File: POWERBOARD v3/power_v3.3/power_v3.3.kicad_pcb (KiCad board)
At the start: 2 copper layers, 46 parts, among them IC1 MAX25301AATB_V+T, J1 2053380003, J2 UJ20-C-H-G-SMT-1-P16-TR, J3 2053380002, U1 USBLC6-2, U2 BQ25886RGE, U3 TPS62160DSG

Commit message: (nearly) finished schematic and layout, beginning routing (hooooooly)
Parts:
- removed C9: 22u, Capacitor_SMD:C_1206_3216Metric
- added C14: 100n, Capacitor_SMD:C_0402_1005Metric, F.Cu at (151.0, 88.2)
- added C15: 100n, Capacitor_SMD:C_0402_1005Metric, F.Cu at (153.5, 88.2)
- added C16: 100n, Capacitor_SMD:C_0402_1005Metric, F.Cu at (151.0, 80.8)
- added C17: 100n, Capacitor_SMD:C_0402_1005Metric, F.Cu at (142.0, 73.0)
- added D5: LED, LED_THT:LED_D5.0mm, F.Cu at (155.5, 72.5)
- added IC2: MCP6541T-I_OT, MCP6541T-I_OT:SOT95P270X145-5N, F.Cu at (152.0, 84.5)
- added IC3: AP2281-1FMG-7, APP2281-1FMG-7:SON50P201X181X60-7N, F.Cu at (142.0, 76.0)
- added R13: 10k, Resistor_SMD:R_0603_1608Metric, B.Cu at (148.5, 94.0)
- added R14: 51.1k, Resistor_SMD:R_0603_1608Metric, B.Cu at (152.2, 79.8)
- added R15: 10k, Resistor_SMD:R_0603_1608Metric, B.Cu at (149.0, 84.2)
- added R16: 26.7k, Resistor_SMD:R_0603_1608Metric, B.Cu at (149.0, 88.1)
- added R17: 10k, Resistor_SMD:R_0603_1608Metric, B.Cu at (147.0, 85.9)
- added R18: 330, Resistor_SMD:R_0603_1608Metric, B.Cu at (156.2, 77.8)
- added S2: MFS201N-9-Z, MFS201N-9-Z:MFS201N9Z, F.Cu at (156.0, 101.0)
- D3, D4, R1, R10, R11, R12, R2, R3, R4, R5, R6, R7: moved to B.Cu
- moved BAT1 48.5 mm to (136.5, 98.0), turned to 180 degrees
- moved J1 39.3 mm to (135.3, 89.7), turned to 90 degrees
- moved GND1 37.9 mm to (186.5, 99.5), turned to 180 degrees
- moved LDO5V1 35.9 mm to (147.0, 72.0), turned to 180 degrees
- moved R12 35.3 mm to (169.8, 92.0)
- moved R11 32.9 mm to (166.9, 87.5), turned to 90 degrees
- moved R10 32.0 mm to (166.9, 91.3), turned to 90 degrees
- moved R1 31.2 mm to (182.5, 96.3), turned to -90 degrees
- moved J3 31.2 mm to (135.2, 76.3), turned to 90 degrees
- moved L2 29.7 mm to (169.9, 93.0), turned to 180 degrees
- moved C12 29.3 mm to (158.5, 85.0), turned to 90 degrees
- moved C11 27.6 mm to (159.5, 90.5), turned to -90 degrees
- moved Cout1 27.2 mm to (172.9, 87.5), turned to 90 degrees
- moved C10 27.0 mm to (163.1, 85.5), turned to 180 degrees
- moved U1 26.9 mm to (187.0, 80.0), turned to 90 degrees
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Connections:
- net /Charging circuit/NTC renamed NTC
- J3 pad 1: /5.3 to 5V/output_at_5 -> Net-(IC3-OUT_1)
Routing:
- net /5.3 to 5V/INCOMP: track 0.00 -> 28.0 mm
- net /5.3 to 5V/output_at_5: track 0.00 -> 25.1 mm, vias 0 -> 2
- net VBUS: track 0.00 -> 17.5 mm
- net /Charging circuit/BATTERY VOLTAGE: track 0.00 -> 11.0 mm
- net /5.3 to 5V/IN: track 0.00 -> 10.5 mm, vias 0 -> 1
- net /Charging circuit/REGN: track 0.00 -> 7.54 mm, vias 0 -> 1
- net NTC: track 0.00 -> 7.02 mm, vias 0 -> 1
- net /Charging circuit/PMID: track 0.00 -> 6.86 mm
- net /Charging circuit/SYS: track 0.00 -> 5.17 mm
- net Net-(D5-K): track 0.00 -> 4.80 mm
- net Net-(U3-FB): track 0.00 -> 4.73 mm, vias 0 -> 1
- net /Charging circuit/ICHGSET: track 0.00 -> 4.67 mm, vias 0 -> 1
- net Net-(IC3-OUT_1): track 0.00 -> 4.60 mm
- net Net-(U3-SW): track 0.00 -> 4.26 mm
- net Net-(U3-PG): track 0.00 -> 4.22 mm, vias 0 -> 1
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- added copper zone on In1.Cu, net GND
- added copper zone on In2.Cu, net GND
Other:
- copper layers 2 -> 4

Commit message: updated routing
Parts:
- moved BAT1 12.8 mm to (126.8, 106.4)
- moved LDO5V1 11.1 mm to (143.2, 82.4), turned to 0 degrees
- moved BUCK5V3 10.3 mm to (169.4, 107.0)
- moved R9 9.17 mm to (188.0, 79.0), turned to 90 degrees
- moved SYS1 8.73 mm to (176.8, 106.6)
- moved R8 7.59 mm to (186.2, 79.0), turned to 90 degrees
- moved D2 6.52 mm to (188.0, 82.2), turned to 90 degrees
- moved GND1 6.20 mm to (188.4, 105.4)
- moved U1 4.97 mm to (182.1, 79.5), turned to -90 degrees
- moved R13 4.09 mm to (147.0, 90.2)
- moved D1 3.42 mm to (186.2, 82.2), turned to -90 degrees
- moved S2 3.17 mm to (155.7, 97.8)
- moved R3 1.62 mm to (184.8, 78.8)
- moved R4 1.17 mm to (178.6, 97.8)
- moved R1 1.05 mm to (182.5, 97.4)
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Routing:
- net /5.3 to 5V/output_at_5: track 25.1 -> 53.1 mm, vias 2 -> 4
- net /5.3 to 5V/INCOMP: track 28.0 -> 11.4 mm
- net /Charging circuit/SW: track 1.43 -> 18.0 mm, vias 0 -> 2
- net /5.3 to 5V/switch_out: track 3.68 -> 18.8 mm, vias 0 -> 2
- net VBUS: track 17.5 -> 3.00 mm
- net GND: track 1.50 -> 10.7 mm, vias 0 -> 47
- net Net-(S1-COM): track 0.00 -> 7.92 mm
- net /Charging circuit/BATTERY VOLTAGE: track 11.0 -> 3.77 mm
- net Net-(IC2-VIN-): track 2.98 -> 7.49 mm, vias 0 -> 1
- net Net-(U3-SW): track 4.26 -> 0.00 mm
- net Net-(S2-NC_2): track 3.88 -> 0.71 mm
- net Net-(J2-DP1): track 0.00 -> 2.88 mm
- net /Charging circuit/ILIM: track 2.53 -> 5.30 mm
- net Net-(J2-DN1): track 0.00 -> 2.62 mm
- net Net-(D2-A): track 2.50 -> 0.00 mm
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- added copper zone on F.Cu, net /5.3 to 5V/IN
- added copper zone on F.Cu, net Net-(U3-SW)
- removed copper zone on In2.Cu, net GND

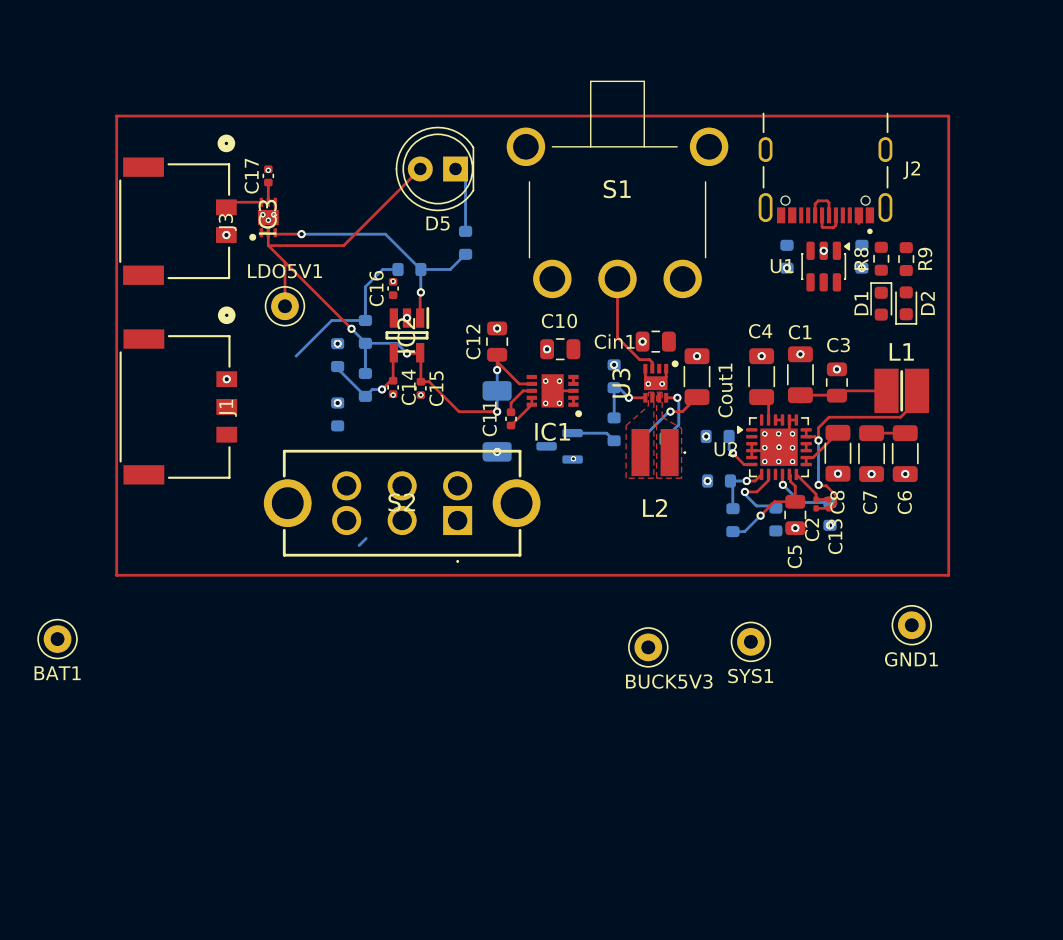
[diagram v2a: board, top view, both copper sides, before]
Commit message: updated routing, added mounting holes
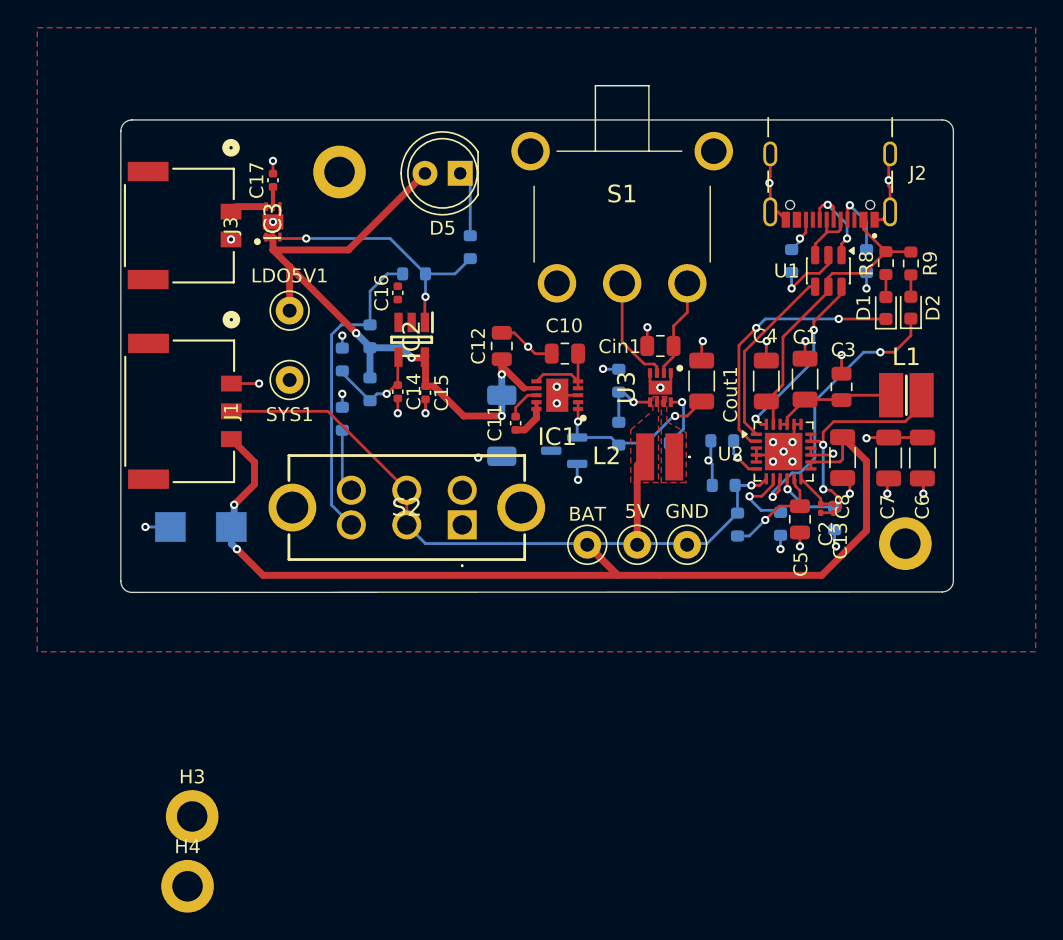
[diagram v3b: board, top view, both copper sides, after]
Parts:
- added D6: SMBJ9.0A, SMBJ9.0A:DIOM5436X261N, B.Cu at (137.1, 98.3)
- added H1: MountingHole, MountingHole:MountingHole_2.2mm_M2_DIN965_Pad, F.Cu at (147.1, 72.7)
- added H2: MountingHole, MountingHole:MountingHole_2.2mm_M2_DIN965_Pad, F.Cu at (187.9, 99.5)
- added H3: MountingHole, MountingHole:MountingHole_2.2mm_M2_DIN965_Pad, F.Cu at (136.5, 119.2)
- added H4: MountingHole, MountingHole:MountingHole_2.2mm_M2_DIN965_Pad, F.Cu at (136.2, 124.2)
- moved BAT 38.8 mm to (165.0, 99.6)
- moved SYS1 38.3 mm to (143.5, 87.7)
- moved GND 17.2 mm to (172.2, 99.6)
- moved 5V 7.44 mm to (168.6, 99.6)
- moved C7 1.27 mm to (186.7, 93.3)
- moved C6 1.27 mm to (189.2, 93.3)
- moved C15 0.46 mm to (153.3, 88.6)
- moved C3 0.46 mm to (183.3, 88.2)
- moved C4 0.46 mm to (177.9, 87.8)
- moved Cout1 0.46 mm to (173.2, 87.8)
- moved R2 0.46 mm to (174.7, 92.1)
- moved R8 0.46 mm to (186.5, 79.3)
- moved S2 0.46 mm to (156.0, 98.2)
- moved C1 0.46 mm to (180.7, 87.7)
- moved C11 0.46 mm to (159.8, 90.8)
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- renumbered BUCK5V3 to 5V, BAT1 to BAT, GND1 to GND
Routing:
- net /Charging circuit/BATTERY VOLTAGE: track 3.77 -> 72.0 mm, vias 0 -> 2
- net GND: track 10.7 -> 62.2 mm, vias 47 -> 37
- net NTC: track 4.52 -> 47.3 mm
- net Net-(D2-K): track 0.00 -> 20.1 mm, vias 0 -> 2
- net VBUS: track 3.00 -> 22.9 mm
- net Net-(D1-K): track 0.00 -> 19.1 mm, vias 0 -> 2
- net /5.3 to 5V/IN: track 9.45 -> 25.6 mm, vias 1 -> 2
- net /Charging circuit/D-: track 0.00 -> 13.4 mm
- net /Charging circuit/D+: track 0.00 -> 13.0 mm, vias 0 -> 2
- net /5.3 to 5V/INCOMP: track 11.4 -> 22.7 mm
- net /Charging circuit/SYS: track 2.93 -> 13.5 mm, vias 0 -> 2
- net /Charging circuit/CC1: track 0.00 -> 4.81 mm, vias 0 -> 1
- net Net-(J2-DP1): track 2.88 -> 7.47 mm, vias 0 -> 2
- net Net-(S2-NC_2): track 0.71 -> 4.59 mm
- net /Charging circuit/CC2: track 0.00 -> 2.58 mm, vias 0 -> 1
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- added copper zone on In2.Cu, net /Charging circuit/SYS
- added copper zone on F.Cu, net GND
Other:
- board outline added: 60 x 34.1 mm

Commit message: added .stp files and extra layout changes, 1 extra mounting hole
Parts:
- removed H4: MountingHole, MountingHole:MountingHole_2.2mm_M2_DIN965_Pad
- moved H3 19.8 mm to (135.6, 99.4)
- moved D6 8.47 mm to (143.0, 92.2)
- moved Cout1 0.95 mm to (174.2, 87.8)
- moved C11 0.88 mm to (160.6, 90.4)
- moved C10 0.67 mm to (164.1, 85.8)
- moved C13 0.67 mm to (183.4, 97.0)
- moved C6 0.67 mm to (189.8, 93.3)
- moved GND1 0.67 mm to (172.9, 99.6)
- moved H1 0.67 mm to (147.8, 72.7)
- moved J1 0.67 mm to (136.3, 90.0)
- moved J2 0.67 mm to (183.2, 68.8)
- moved L1 0.67 mm to (188.7, 88.8)
- moved R14 0.67 mm to (153.2, 80.1)
- moved R3 0.67 mm to (185.8, 79.1)
- moved U1 0.67 mm to (183.1, 79.9)
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- renumbered BAT to BAT1, 5V to BUCK5V3, GND to GND1
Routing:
- net /5.3 to 5V/IN: track 25.6 -> 35.6 mm, vias 2 -> 8
- net VBUS: track 22.9 -> 29.5 mm
- net /5.3 to 5V/output_at_5: track 53.5 -> 59.6 mm
- net /5.3 to 5V/INCOMP: track 22.7 -> 27.2 mm, vias 0 -> 1
- net Net-(U3-SW): track 0.00 -> 4.26 mm
- net Net-(S2-NO_1): track 0.00 -> 2.50 mm
- net GND: track 62.2 -> 64.7 mm
- net /Charging circuit/BATTERY VOLTAGE: track 72.0 -> 70.0 mm
- net NTC: track 47.3 -> 49.0 mm
- net /Charging circuit/SW: track 18.0 -> 18.5 mm

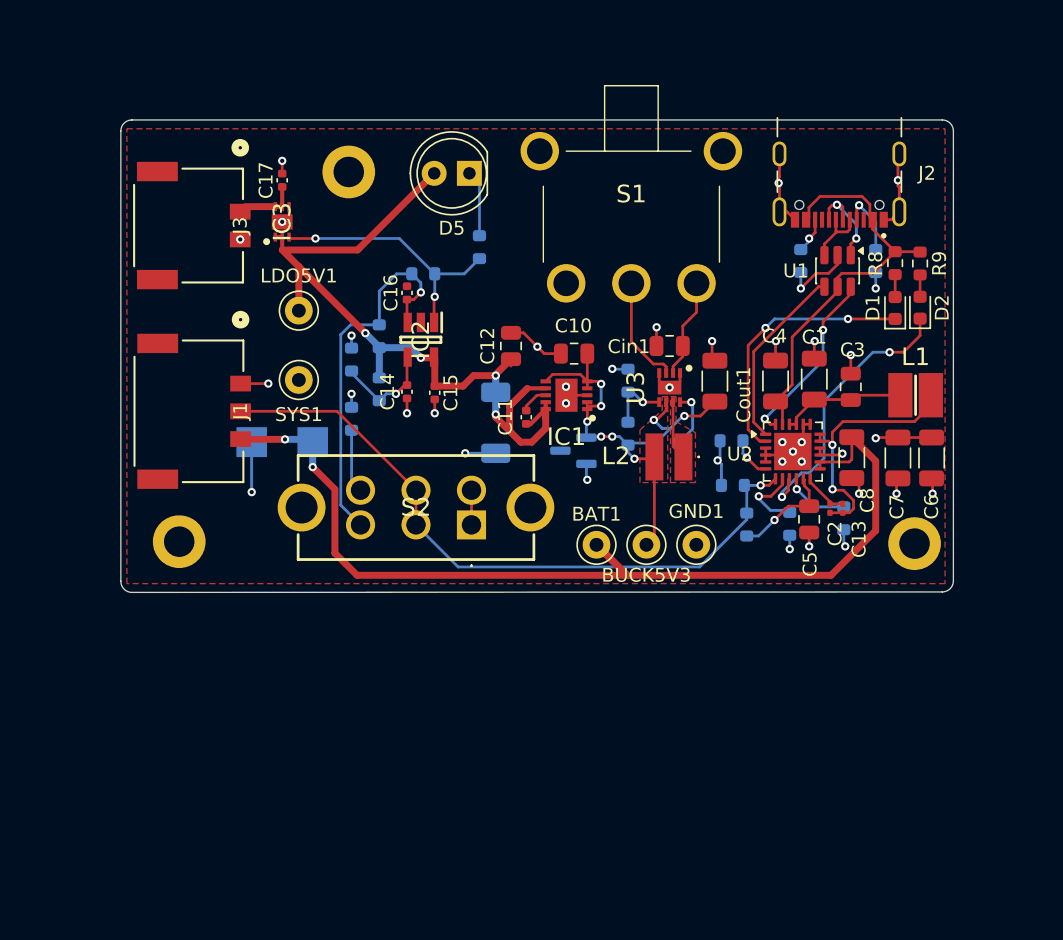
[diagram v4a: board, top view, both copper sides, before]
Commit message: changed battery connection
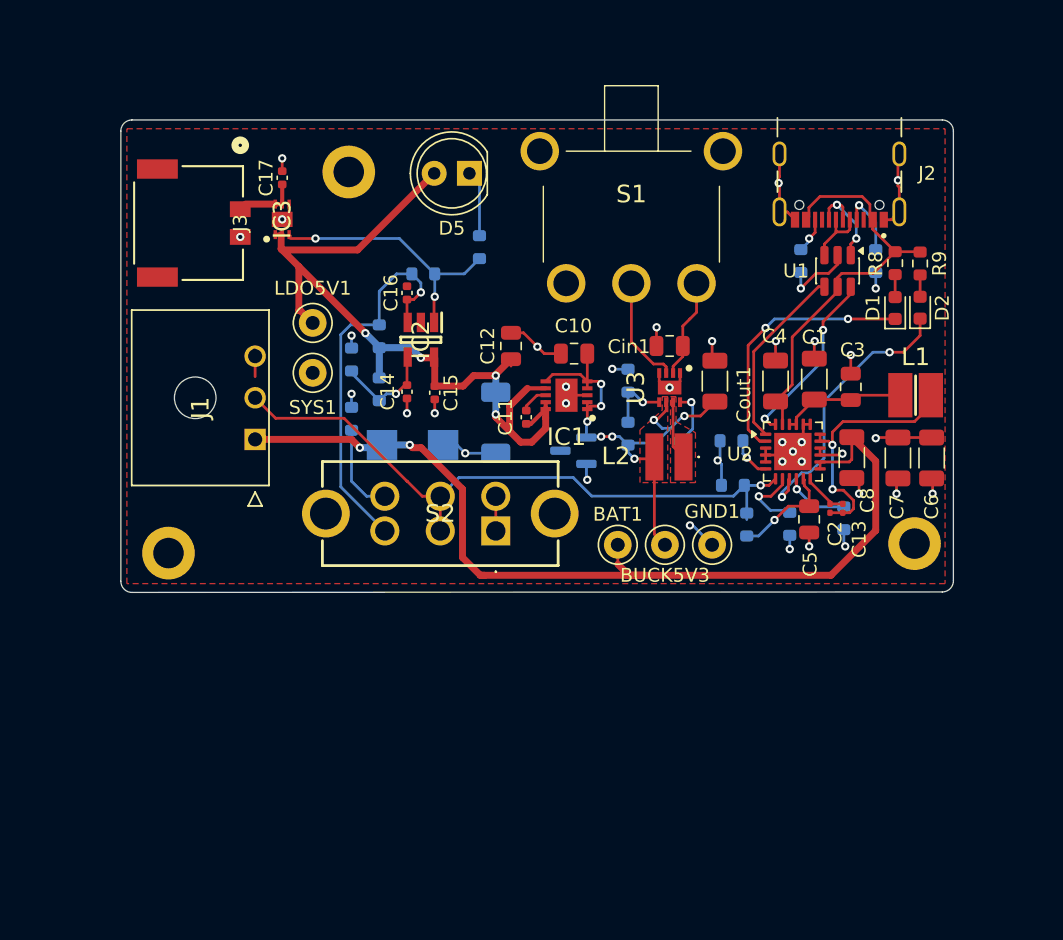
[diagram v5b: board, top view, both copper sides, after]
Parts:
- J1: value 2053380003 -> 43650-0300; footprint footprintsusbc:CONN_2053380000-SD_03_MOL -> bat_connect_new:436500300
- moved D6 9.40 mm to (152.4, 92.4), turned to 0 degrees
- moved J1 5.19 mm to (141.0, 92.0), turned to -90 degrees
- moved S2 1.80 mm to (158.4, 98.6)
- moved BAT1 1.53 mm to (167.2, 99.6)
- moved LDO5V1 1.34 mm to (145.2, 83.6)
- moved BUCK5V3 1.34 mm to (170.6, 99.6)
- moved GND1 1.13 mm to (174.0, 99.6)
- moved H3 1.13 mm to (134.8, 100.2)
- moved SYS1 1.12 mm to (145.2, 87.2)
- moved J3 0.18 mm to (136.2, 76.4)
- moved C17 0.18 mm to (143.0, 73.1)
- moved IC3 0.18 mm to (143.0, 76.1)
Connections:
- J1 pad 1: GND -> /Charging circuit/BATTERY VOLTAGE
- J1 pad 3: /Charging circuit/BATTERY VOLTAGE -> GND
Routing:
- net Net-(S2-NC_2): track 4.59 -> 6.52 mm
- net NTC: track 49.0 -> 47.3 mm
- net /5.3 to 5V/output_at_5: track 59.6 -> 61.3 mm
- net /5.3 to 5V/INCOMP: track 27.2 -> 28.3 mm
